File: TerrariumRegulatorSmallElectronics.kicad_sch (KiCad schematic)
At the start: 24 parts, among them J101 Barrel_Jack, J102 USB_B_Micro, J103 Conn_01x03, J104 Conn_01x03, J105 Conn_02x05_Odd_Even, SW101 SW_Push, U101 LTC1174CS8_PBF, U102 STM32F103RBTx, U103 DHT11, Y101 Crystal

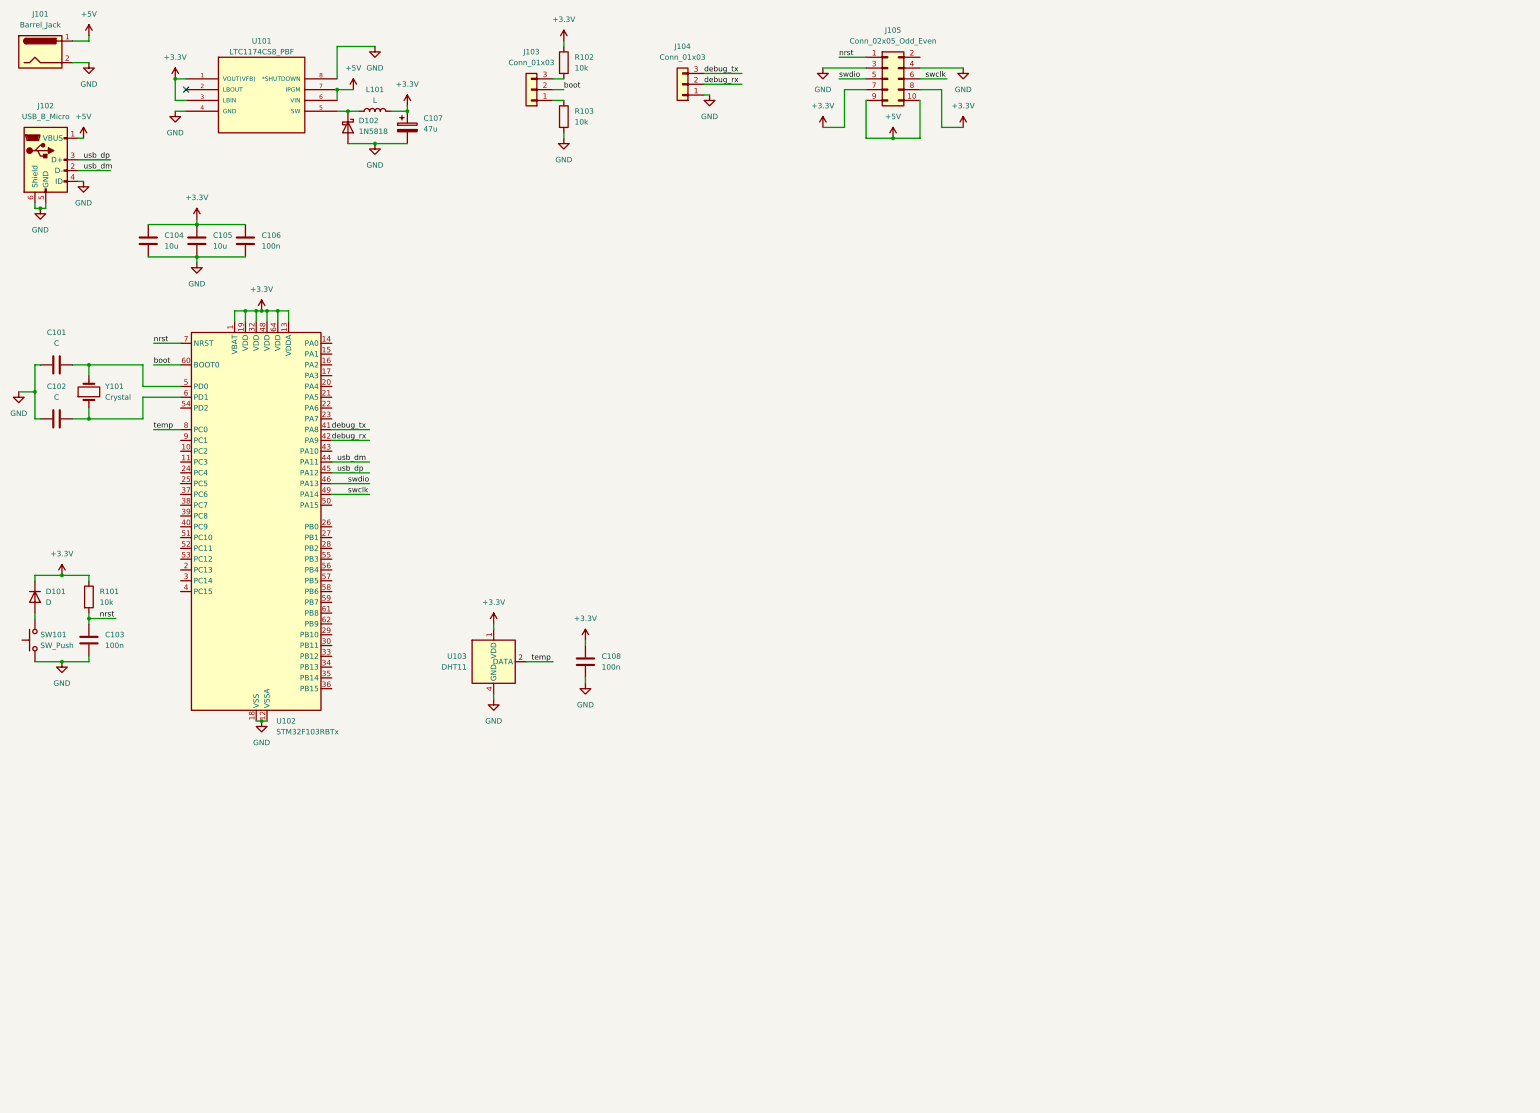
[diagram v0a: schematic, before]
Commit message: Added display symbol
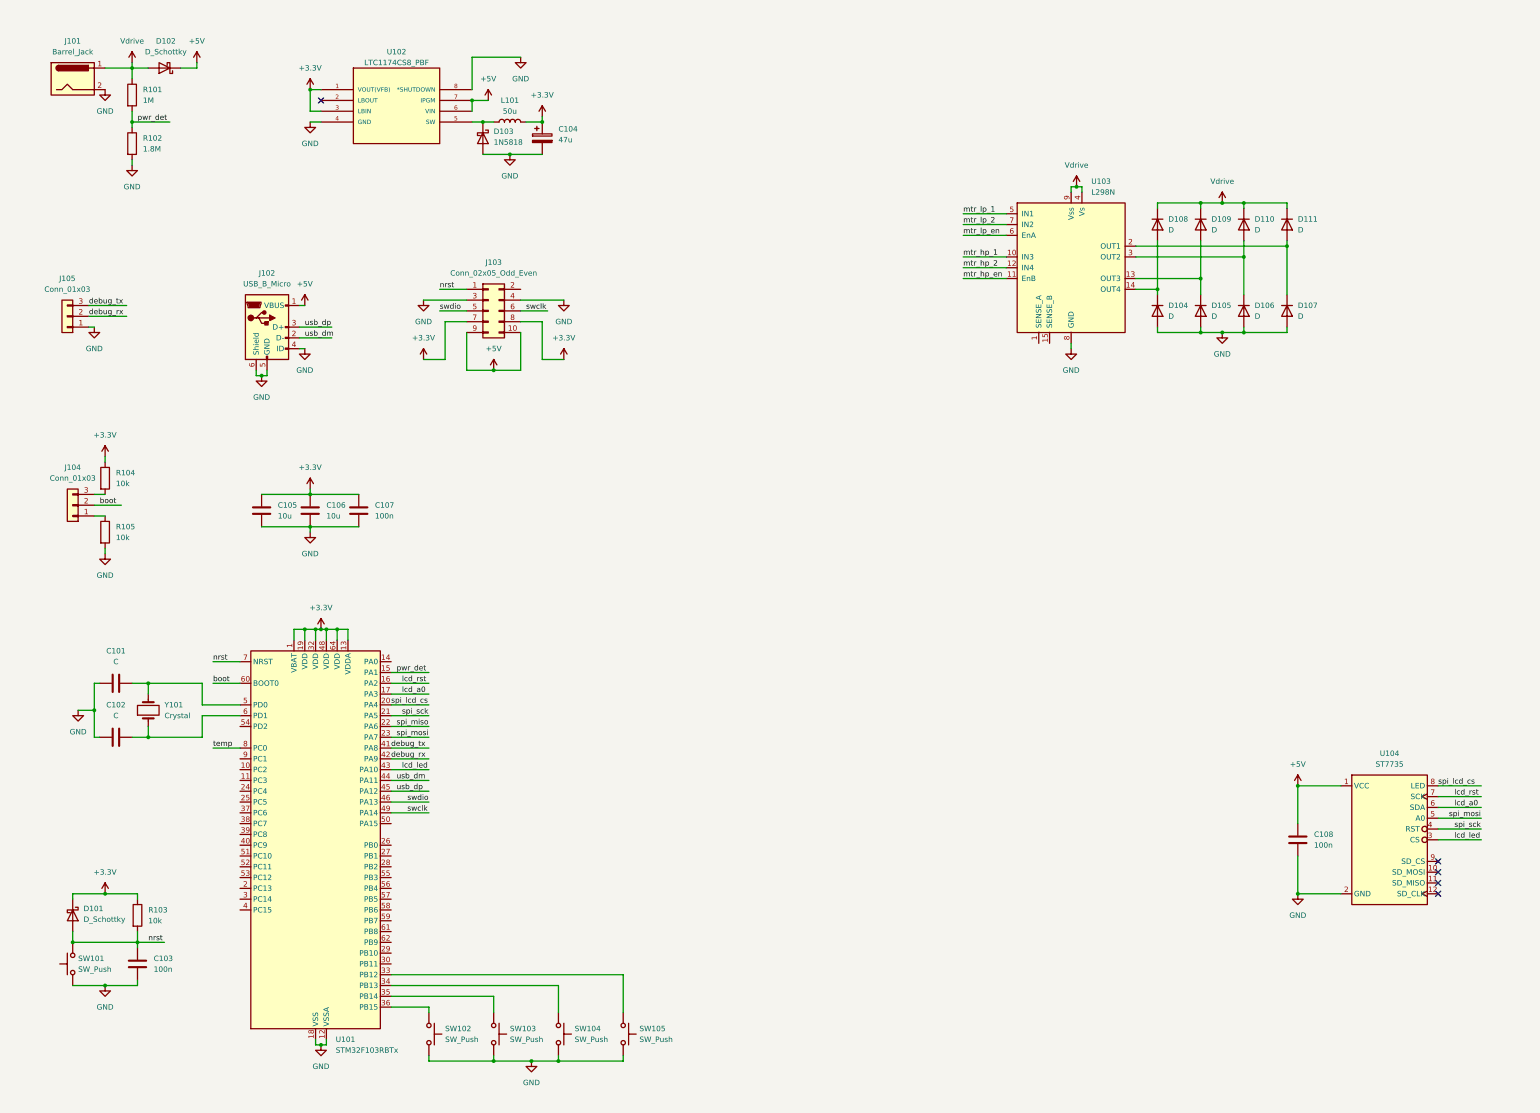
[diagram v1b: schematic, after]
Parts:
- removed D101: D, symbol Device:D
- removed U103: DHT11, Sensor:Aosong_DHT11_5.5x12.0_P2.54mm, symbol Sensor:DHT11
- added D101, D102: D_Schottky, symbol Device:D_Schottky
- added D104, D105, D106, D107, D108, D109, D110, D111: D, symbol Device:D
- added R101: 1M, symbol Device:R
- added R102: 1.8M, symbol Device:R
- added SW102, SW103, SW104, SW105: SW_Push, symbol Switch:SW_Push
- added U103: L298N, Package_TO_SOT_THT:TO-220-15_P2.54x2.54mm_StaggerOdd_Lead4.58mm_Vertical, symbol Driver_Motor:L298N
- added U104: ST7735, symbol Display:ST7735
- L101: value L -> 50u
- renumbered C107 to C104, C104 to C105, C105 to C106, C106 to C107, D102 to D103, J105 to J103, J103 to J104, J104 to J105, R101 to R103, R102 to R104, R103 to R105, U102 to U101, U101 to U102
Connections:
- net +3.3V: now also D101.1 (K); no longer C108.1
- net +5V: now also C108.1, D102.1 (K), U104.1 (VCC); no longer J101.1
- net GND: now also D104.2 (A), D105.2 (A), D106.2 (A), D107.2 (A), R102.2, SW102.2, SW103.2, SW104.2, SW105.2, U103.8 (GND), U104.2 (GND)
- net nrst: now also SW101.2, D101.2 (A)
- net pwr_det: now reaches U101.15 (PA1)
- net pwr_det: now also R101.2, R102.1
- net lcd_rst: now reaches U101.16 (PA2)
- net lcd_rst: now also U104.7 (SCK)
- net lcd_a0: now reaches U101.17 (PA3)
- net lcd_a0: now also U104.6 (SDA)
- net spi_lcd_cs: now reaches U101.20 (PA4)
- net spi_lcd_cs: now also U104.8 (LED)
- net spi_sck: now reaches U101.21 (PA5)
- net spi_sck: now also U104.4 (RST)
- net spi_miso: now reaches U101.22 (PA6)
- net spi_mosi: now reaches U101.23 (PA7)
- net spi_mosi: now also U104.5 (A0)
- net at U101.33 (PB12): now also SW105.1
- net at U101.34 (PB13): now also SW104.1
- net at U101.35 (PB14): now also SW103.1
- net at U101.36 (PB15): now also SW102.1
- net lcd_led: now reaches U101.43 (PA10)
- net lcd_led: now also U104.3 (CS)
- new net: D107.1 (K), D111.2 (A), U103.2 (OUT1)
- new net: D105.1 (K), D109.2 (A), U103.13 (OUT3)
- new net: D104.1 (K), D108.2 (A), U103.14 (OUT4)
- new net: D106.1 (K), D110.2 (A), U103.3 (OUT2)
- new net Vdrive: D102.2 (A), D108.1 (K), D109.1 (K), D110.1 (K), D111.1 (K), J101.1, R101.1, U103.4 (Vs), U103.9 (Vss)
- new net mtr_hp_1: U103.10 (IN3)
- new net mtr_hp_2: U103.12 (IN4)
- new net mtr_hp_en: U103.11 (EnB)
- new net mtr_lp_1: U103.5 (IN1)
- new net mtr_lp_2: U103.7 (IN2)
- new net mtr_lp_en: U103.6 (EnA)
- no-connect marks 1 -> 5
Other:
- title: (none) -> TerrariumController
- moved on the sheet: C101, C102, C103, C104, C105, C106, C107, D103, J101, J102, J103, J104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

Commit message: Fixed buck circuit and added motor drive
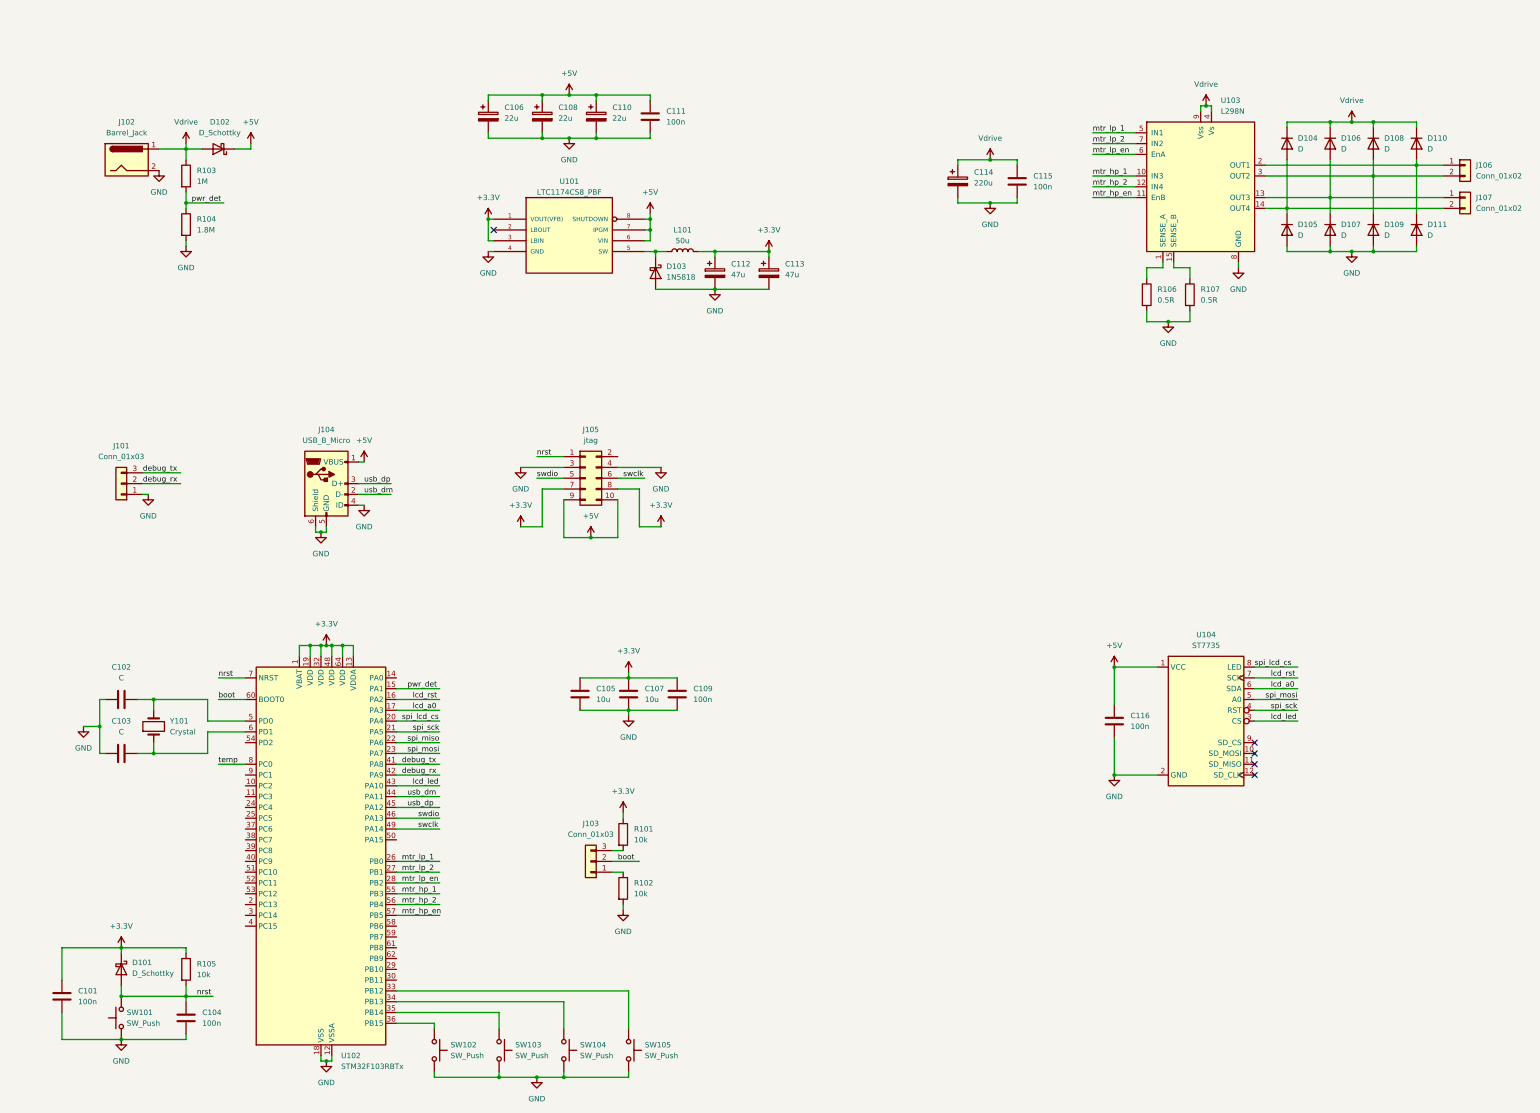
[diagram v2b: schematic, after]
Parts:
- added C101, C111, C115: 100n, symbol Device:C
- added C106, C108, C110: 22u, symbol Device:C_Polarized
- added C113: 47u, symbol Device:C_Polarized
- added C114: 220u, symbol Device:C_Polarized
- added J106, J107: Conn_01x02, symbol Connector_Generic:Conn_01x02
- added R106, R107: 0.5R, symbol Device:R
- J105: renamed from J103; value Conn_02x05_Odd_Even -> jtag
- renumbered C101 to C102, C102 to C103, C103 to C104, C106 to C107, C107 to C109, C104 to C112, C108 to C116, D108 to D104, D104 to D105, D109 to D106, D105 to D107, D110 to D108, D106 to D109, D111 to D110, D107 to D111, J105 to J101, J101 to J102, J104 to J103, J102 to J104, R104 to R101, R105 to R102, R101 to R103, R102 to R104, R103 to R105, U102 to U101, U101 to U102
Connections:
- net +3.3V: now also C101.1, C113.1
- net +5V: now also U101.8 (SHUTDOWN), C106.1, C108.1, C110.1, C111.1
- net GND: now also C101.2, C106.2, C108.2, C110.2, C111.2, C113.2, C114.2, C115.2, R106.2, R107.2; no longer U101.8 (*SHUTDOWN)
- net Vdrive: now also C114.1, C115.1
- net mtr_hp_1: now also U102.55 (PB3)
- net mtr_hp_2: now also U102.56 (PB4)
- net mtr_hp_en: now also U102.57 (PB5)
- net mtr_lp_1: now also U102.26 (PB0)
- net mtr_lp_2: now also U102.27 (PB1)
- net mtr_lp_en: now also U102.28 (PB2)
- net at D110.2 (A), D111.1 (K), U103.2 (OUT1): now also J106.1 (Pin_1)
- net at U103.1 (SENSE_A): now also R106.1
- net at D106.2 (A), D107.1 (K), U103.13 (OUT3): now also J107.1 (Pin_1)
- net at D104.2 (A), D105.1 (K), U103.14 (OUT4): now also J107.2 (Pin_2)
- net at U103.15 (SENSE_B): now also R107.1
- net at D108.2 (A), D109.1 (K), U103.3 (OUT2): now also J106.2 (Pin_2)
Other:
- moved on the sheet: C102, C103, C104, C105, C107, C109, C112, C116, D101, D102, D103, D104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

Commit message: ERC fixes
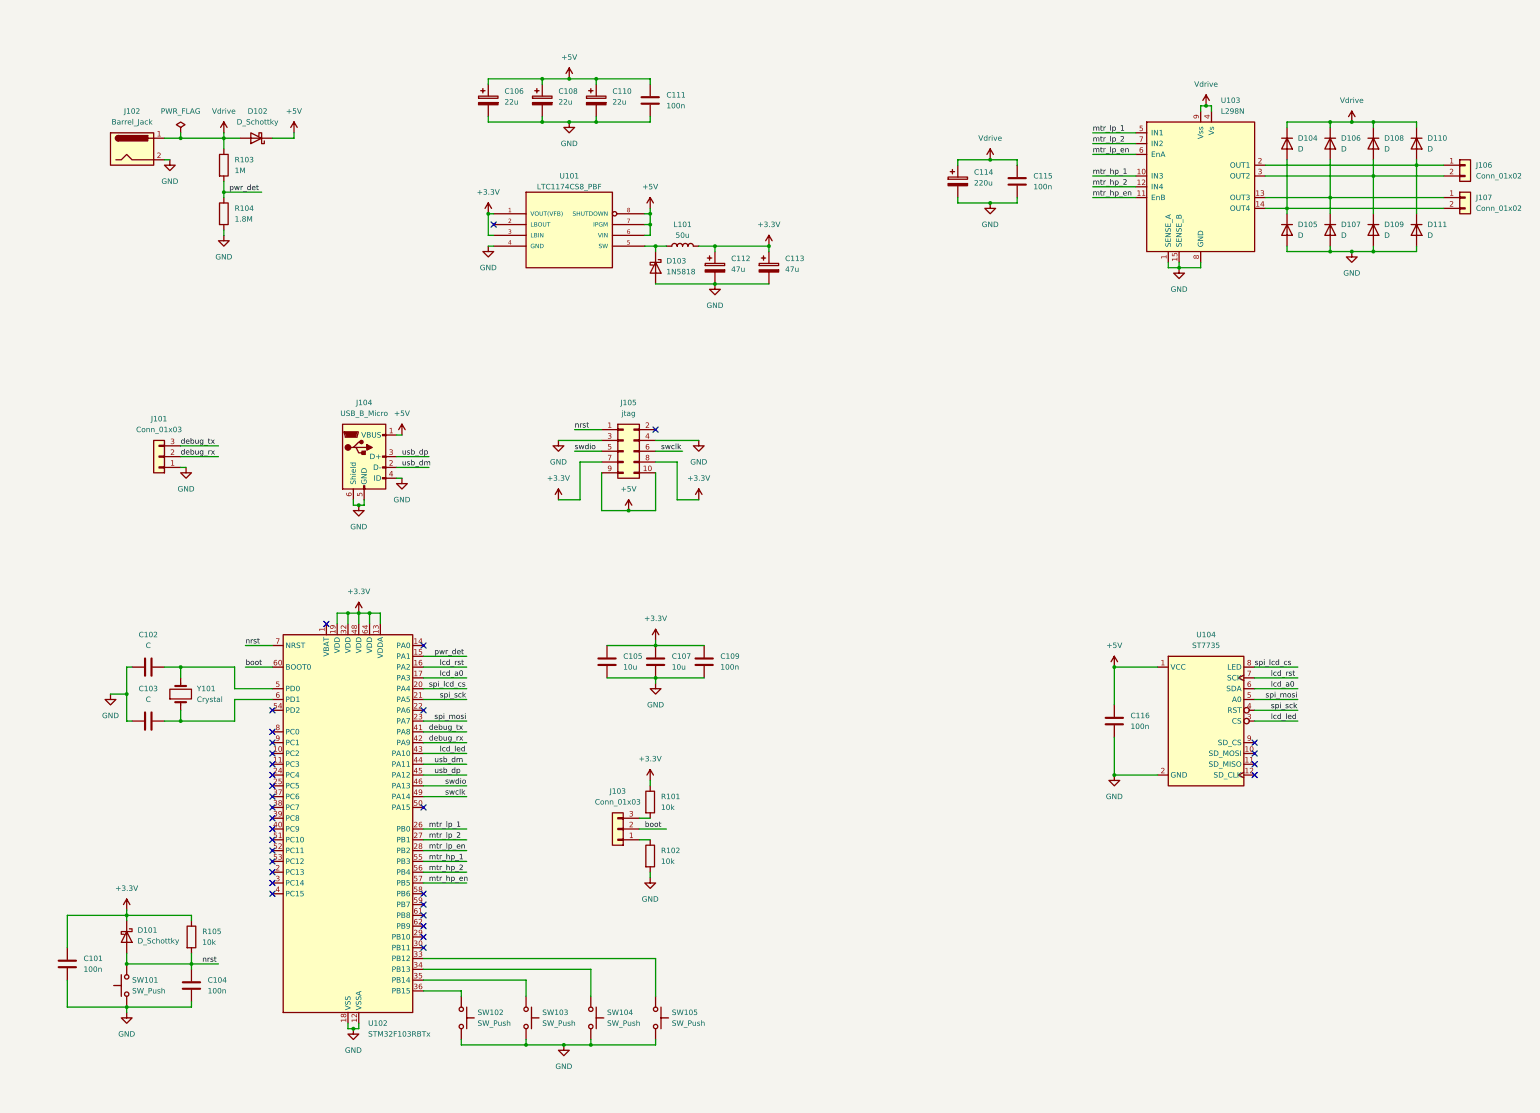
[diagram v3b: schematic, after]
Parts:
- removed R106, R107: 0.5R, symbol Device:R
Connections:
- net +3.3V: no longer U102.1 (VBAT)
- net GND: now also U103.1 (SENSE_A), U103.15 (SENSE_B)
- net spi_miso: no longer names the net of U102.22 (PA6)
- net temp: no longer names the net of U102.8 (PC0)
- no-connect marks 5 -> 33
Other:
- moved on the sheet: C101, C102, C103, C104, C105, C106, C107, C108, C109, C110, C111, C112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
